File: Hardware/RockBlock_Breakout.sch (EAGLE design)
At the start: 5 parts, among them U1 ATMEGA328P_TQFP, U2 NC7SZ157SC-70, U3 NC7SZ157SC-70

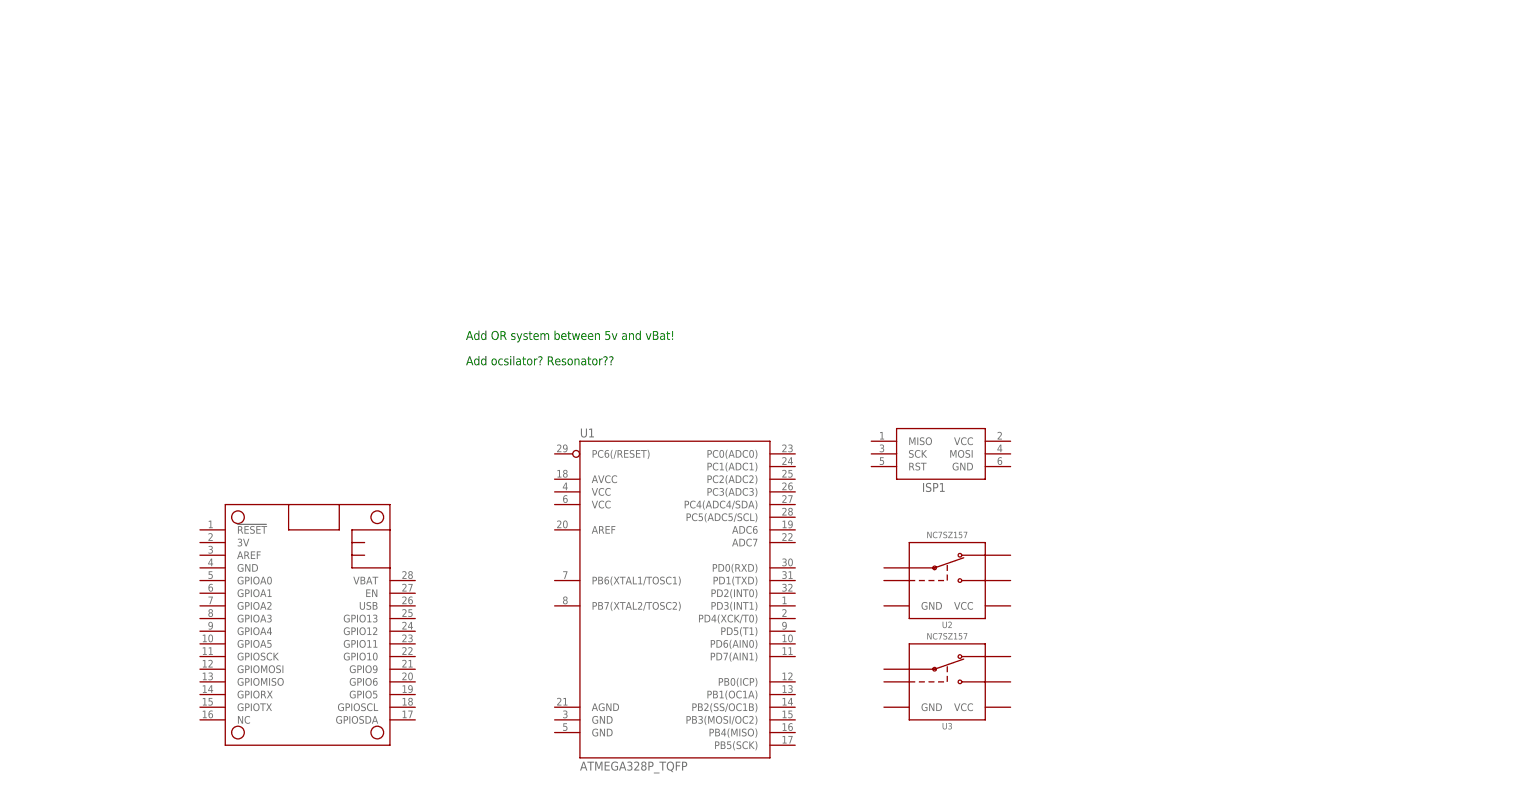
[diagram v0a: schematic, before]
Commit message: Preliminary layout of RockBlock Breakout
Still needs cleanup and some verification
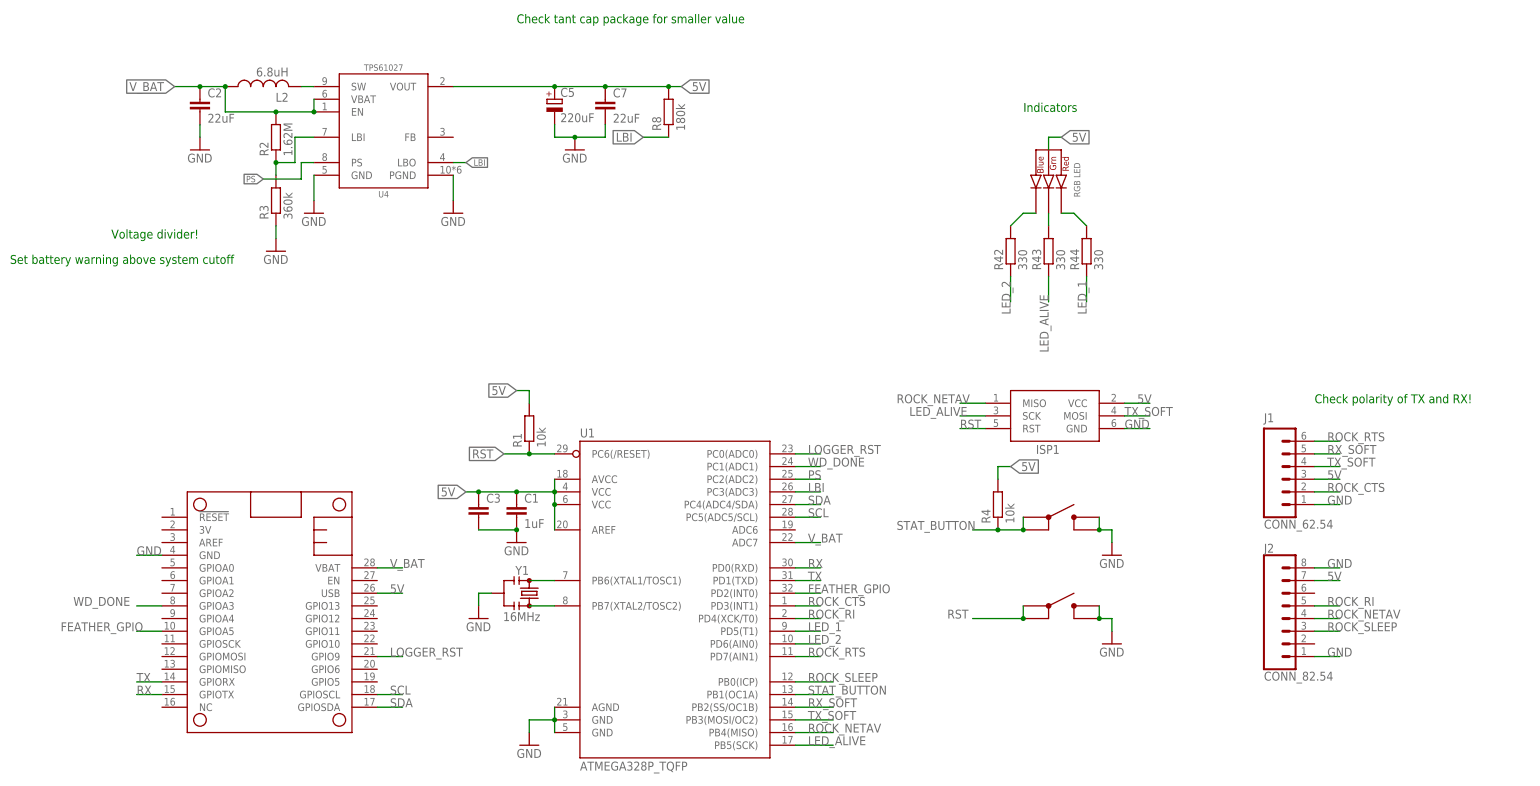
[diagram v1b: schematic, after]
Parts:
- removed U2, U3: NC7SZ157SC-70, bschulz:NC7SZ157SC-70
- added C1: 1uF, bschulz_passives:C-EUC0603
- added C2, C7: 22uF, bschulz_passives:C-EU22UFC0805
- added C3: (no value), bschulz_passives:C-EUC0402
- added C5: 220uF, bschulz_passives:CTANT_EU2917
- added D5: CLVBA-FKA, bschulz:CLVBA-FKA
- added J1: CONN_62.54, bschulz:CONN_62.54
- added J2: CONN_82.54, bschulz:CONN_82.54
- added L2: 6.8uH, bschulz:INDUCTORTPC_4.8X4.8
- added R1, R4: 10k, bschulz_passives:R-EU_R0402
- added R2: 1.62M, bschulz_passives:R-EU_1.62MR0603
- added R3: 360k, bschulz_passives:R-EU_360KR0603
- added R42, R43, R44: 330, bschulz_passives:R-EU_330R0402
- added R8: 180k, bschulz_passives:R-EU_180KR0603
- added S1, S2: BUTTON4.2X3.2, bschulz:BUTTON4.2X3.2
- added U4: TPS61027DRC, bschulz:TPS61027DRC
- added Y1: 16MHz, bschulz:RESONATOR16MHZSMD_3.2X1.3
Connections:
- new net 5V: C1.1, C3.1, C5.+, C7.1, D5.ANODE, ISP1.VCC, J1.3, J2.7, MS1.USB, R1.2, R4.2, R8.2, U1.AREF, U1.AVCC, U1.VCC@4, U1.VCC@6, U4.VOUT
- new net FEATHER_GPIO: MS1.GPIOA5, U1.PD2(INT0)
- new net GND: C1.2, C2.2, C3.2, C5.-, C7.2, ISP1.GND, J1.1, J2.1, J2.8, MS1.GND, R3.1, S1.3, S1.4, S2.3, S2.4, U1.AGND, U1.GND@3, U1.GND@5, U4.GND, U4.PGND, Y1.2
- new net LBI: R8.1, U1.PC3(ADC3), U4.LBO
- new net LED_1: R44.1, U1.PD5(T1)
- new net LED_2: R42.1, U1.PD6(AIN0)
- new net LED_ALIVE: ISP1.SCK, R43.1, U1.PB5(SCK)
- new net LOGGER_RST: MS1.GPIO9, U1.PC0(ADC0)
- new net N$2: U1.PB6(XTAL1/TOSC1), Y1.1
- new net N$3: U1.PB7(XTAL2/TOSC2), Y1.3
- new net N$4: R2.1, R3.2, U4.LBI
- new net N$5: L2.2, U4.SW
- new net N$58: D5.BLUE_CATH, R42.2
- new net N$59: D5.GREEN_CATH, R43.2
- new net N$60: D5.RED_CATH, R44.2
- new net PS: U1.PC2(ADC2), U4.PS
- new net ROCK_CTS: J1.2, U1.PD3(INT1)
- new net ROCK_NETAV: ISP1.MISO, J2.4, U1.PB4(MISO)
- new net ROCK_RI: J2.5, U1.PD4(XCK/T0)
- new net ROCK_RTS: J1.6, U1.PD7(AIN1)
- new net ROCK_SLEEP: J2.3, U1.PB0(ICP)
- new net RST: ISP1.RST, R1.1, S2.1, S2.2, U1.PC6(/RESET)
- new net RX: MS1.GPIOTX, U1.PD0(RXD)
- new net RX_SOFT: J1.5, U1.PB2(SS/OC1B)
- new net SCL: MS1.GPIOSCL, U1.PC5(ADC5/SCL)
- new net SDA: MS1.GPIOSDA, U1.PC4(ADC4/SDA)
- new net STAT_BUTTON: R4.1, S1.1, S1.2, U1.PB1(OC1A)
- new net TX: MS1.GPIORX, U1.PD1(TXD)
- new net TX_SOFT: ISP1.MOSI, J1.4, U1.PB3(MOSI/OC2)
- new net V_BAT: C2.1, L2.1, MS1.VBAT, R2.2, U1.ADC7, U4.EN, U4.VBAT
- new net WD_DONE: MS1.GPIOA3, U1.PC1(ADC1)
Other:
- note added: "Check polarity of TX and RX!"
- note added: "Check tant cap package for smaller value"
- note added: "Indicators"
- note added: "Set battery warning above system cutoff"
- note added: "Voltage divider!"
- note removed: "Add OR system between 5v and vBat!"
- note removed: "Add ocsilator? Resonator??"
- moved on the sheet: ISP1
